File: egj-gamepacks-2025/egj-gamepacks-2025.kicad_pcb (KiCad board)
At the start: 2 copper layers, 52.3 x 64 mm, 83 parts, among them J1 USB_B_Micro, J3 BM03B-SRSS-TB, J5 GameBoy_GamePak_AGB-002, SW1 PTS810SJG250SMTRLFS, SW2 PTS810SJG250SMTRLFS, U1 W25Q128JVSIQ, U10 TPD6E05U06RVZR, U11 VL6180V1NR/1, U12 TXS0108EPW, U13 XC6206P282MR, U14 BNO055, U2 DNF, U3 NCP1117-3.3_SOT223, U4 RP2350_80QFN, U5 USBLC6-2P6, U6 TPD6E05U06RVZR, U7 TPD6E05U06RVZR, U8 TPD6E05U06RVZR, U9 TPD6E05U06RVZR, Y1 ABM8-272-T3

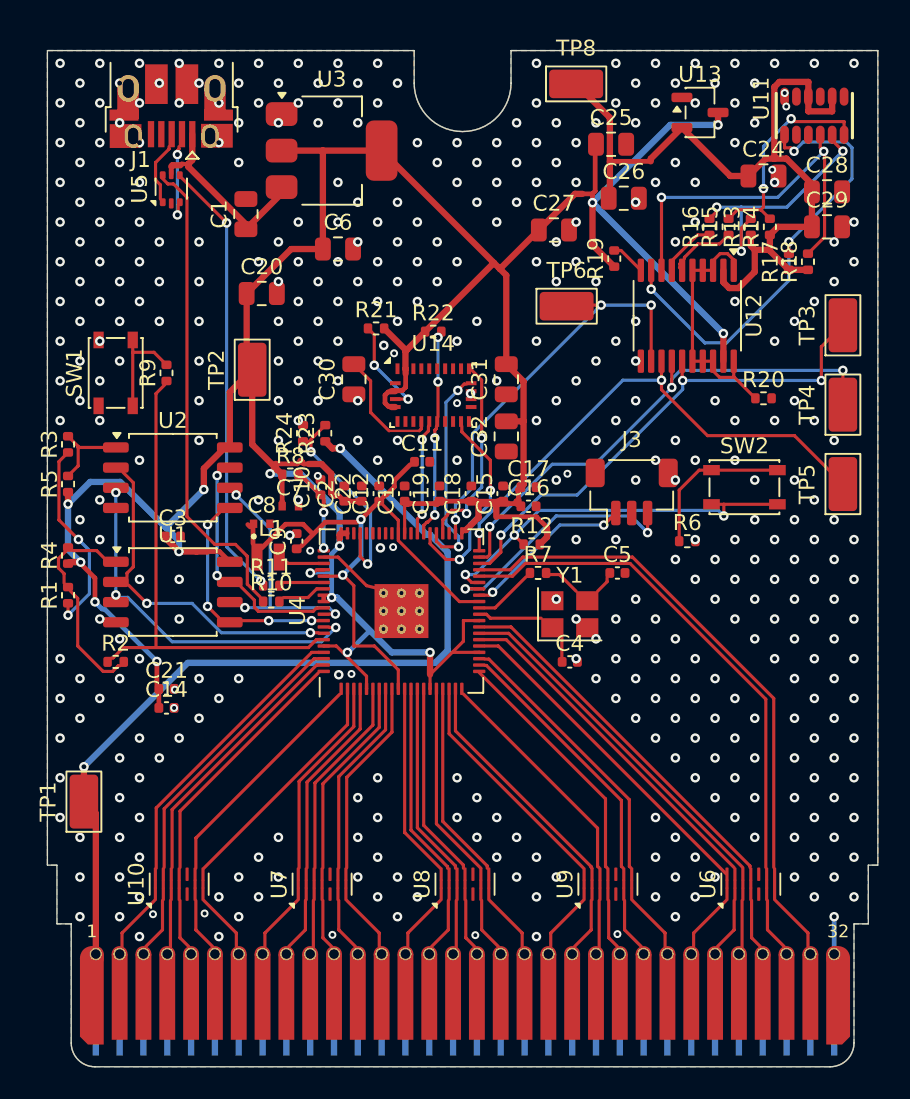
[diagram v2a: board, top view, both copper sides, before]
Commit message: UPDATE: rework RP2350 regulator layout, power path routing, finger tab clearance and silkscreen
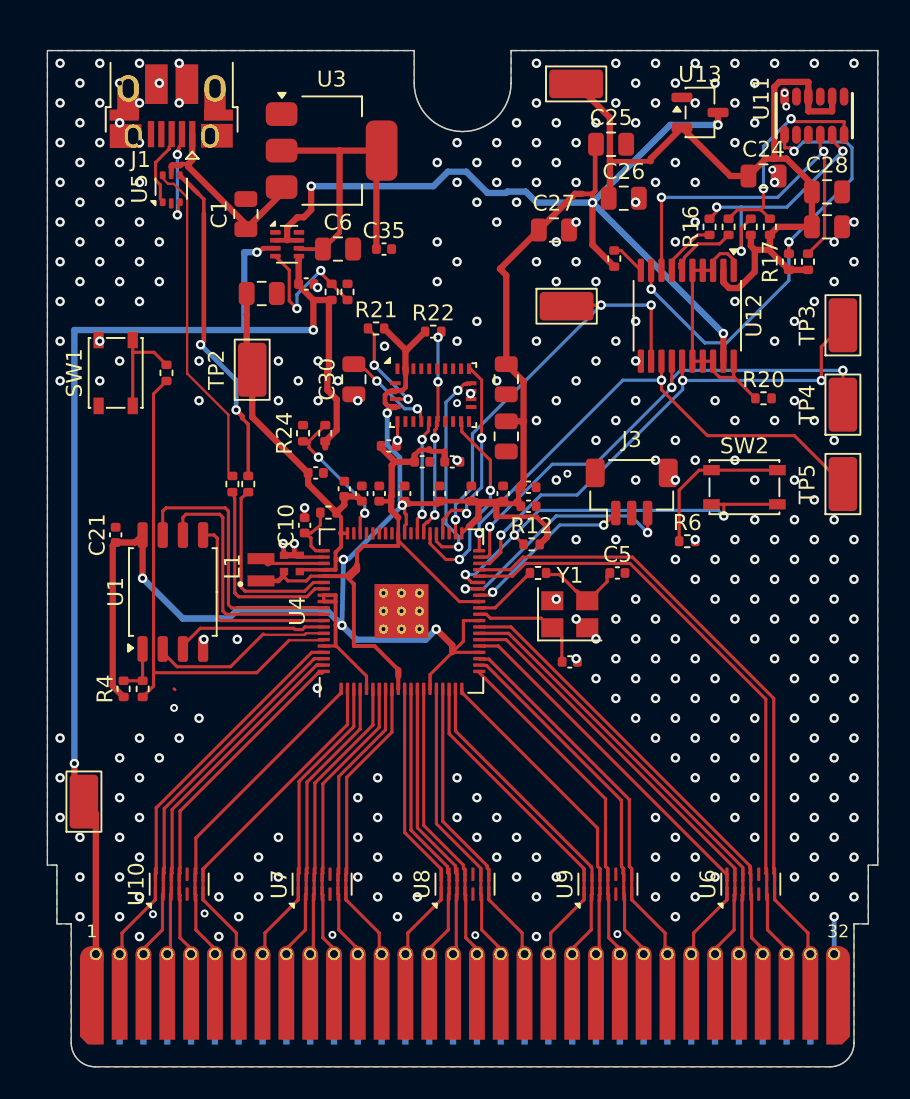
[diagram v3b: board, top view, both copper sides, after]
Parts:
- removed C3: DNF, Capacitor_SMD:C_0402_1005Metric
- removed R1, R3, R5: DNF, Resistor_SMD:R_0402_1005Metric
- removed U2: DNF, Package_SO:SOIC-8_5.3x5.3mm_P1.27mm
- added C33: 100n, Capacitor_SMD:C_0402_1005Metric, F.Cu at (247.2, 86.6)
- added C34: 1u, Capacitor_SMD:C_0402_1005Metric, F.Cu at (238.0, 75.4)
- added C35: 1u, Capacitor_SMD:C_0402_1005Metric, F.Cu at (242.9, 73.2)
- added R25: 180K, Resistor_SMD:R_0402_1005Metric, F.Cu at (239.6, 75.9)
- added R26: 100K, Resistor_SMD:R_0402_1005Metric, F.Cu at (240.6, 75.9)
- added U15: TPS2116DRL, Package_TO_SOT_SMD:SOT-583-8, F.Cu at (236.8, 72.9)
- L1: value 3.3u -> AOTA-B201610S3R3-101-T
- R13, R14: value 4.7K -> 10K
- R17, R18: value 4.7K -> 47K
- moved C14 17.5 mm to (238.6, 87.3)
- moved C21 10.2 mm to (226.0, 91.2), turned to 90 degrees
- moved R4 9.10 mm to (226.5, 100.9)
- moved C9 8.35 mm to (243.2, 85.6), turned to 0 degrees
- moved R10 7.80 mm to (233.3, 88.0), turned to -90 degrees
- moved R11 6.56 mm to (234.3, 88.0), turned to -90 degrees
- moved C7 3.65 mm to (237.6, 93.0), turned to 90 degrees
- moved R8 3.39 mm to (239.4, 89.8), turned to 180 degrees
- moved C8 2.87 mm to (236.6, 93.0), turned to 90 degrees
- moved C10 2.60 mm to (237.9, 90.6)
- moved R2 2.40 mm to (227.7, 100.9), turned to 90 degrees
- moved L1 0.92 mm to (235.2, 93.4), turned to 90 degrees
- moved C2 0.30 mm to (240.4, 88.3)
- turned U1 to 90 degrees
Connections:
- C6 pad 1: +3V3 -> /Power/+3V3_USB
- U3 pad 2: +3V3 -> /Power/+3V3_USB
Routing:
- net +3V3_GBA: track 54.8 -> 78.0 mm, vias 2 -> 3
- net /Power/+3V3_USB: track 0.00 -> 20.8 mm
- net +3V3: track 223.0 -> 204.8 mm, vias 15 -> 10
- net /RP2350/GPIO0: track 12.6 -> 0.00 mm, vias 2 -> 0
- net /RP2350/QSPI_SD2: track 22.1 -> 9.64 mm, vias 3 -> 0
- net Net-(U4-USB_DP): track 2.43 -> 12.3 mm
- net Net-(U4-USB_DM): track 2.20 -> 11.7 mm
- net /RP2350/USB_D+: track 29.9 -> 20.4 mm
- net Net-(U15-PR1): track 0.00 -> 9.42 mm, vias 0 -> 2
- net /RP2350/QSPI_SD1: track 20.2 -> 11.6 mm, vias 2 -> 0
- net /RP2350/FLASH_SS: track 11.6 -> 3.20 mm
- net +1V1: track 36.2 -> 43.1 mm, vias 2 -> 0
- net /RP2350/USB_D-: track 27.4 -> 20.9 mm
- net /RP2350/FLASH2_SS: track 5.40 -> 0.00 mm
- net /RP2350/QSPI_SD3: track 12.6 -> 17.8 mm, vias 2 -> 0
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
